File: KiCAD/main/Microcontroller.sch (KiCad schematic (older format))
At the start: 10 parts, among them J5 Conn_02x04_Odd_Even, SW2 BOOT, SW3 RESET, U3 ESP32-WROOM-32

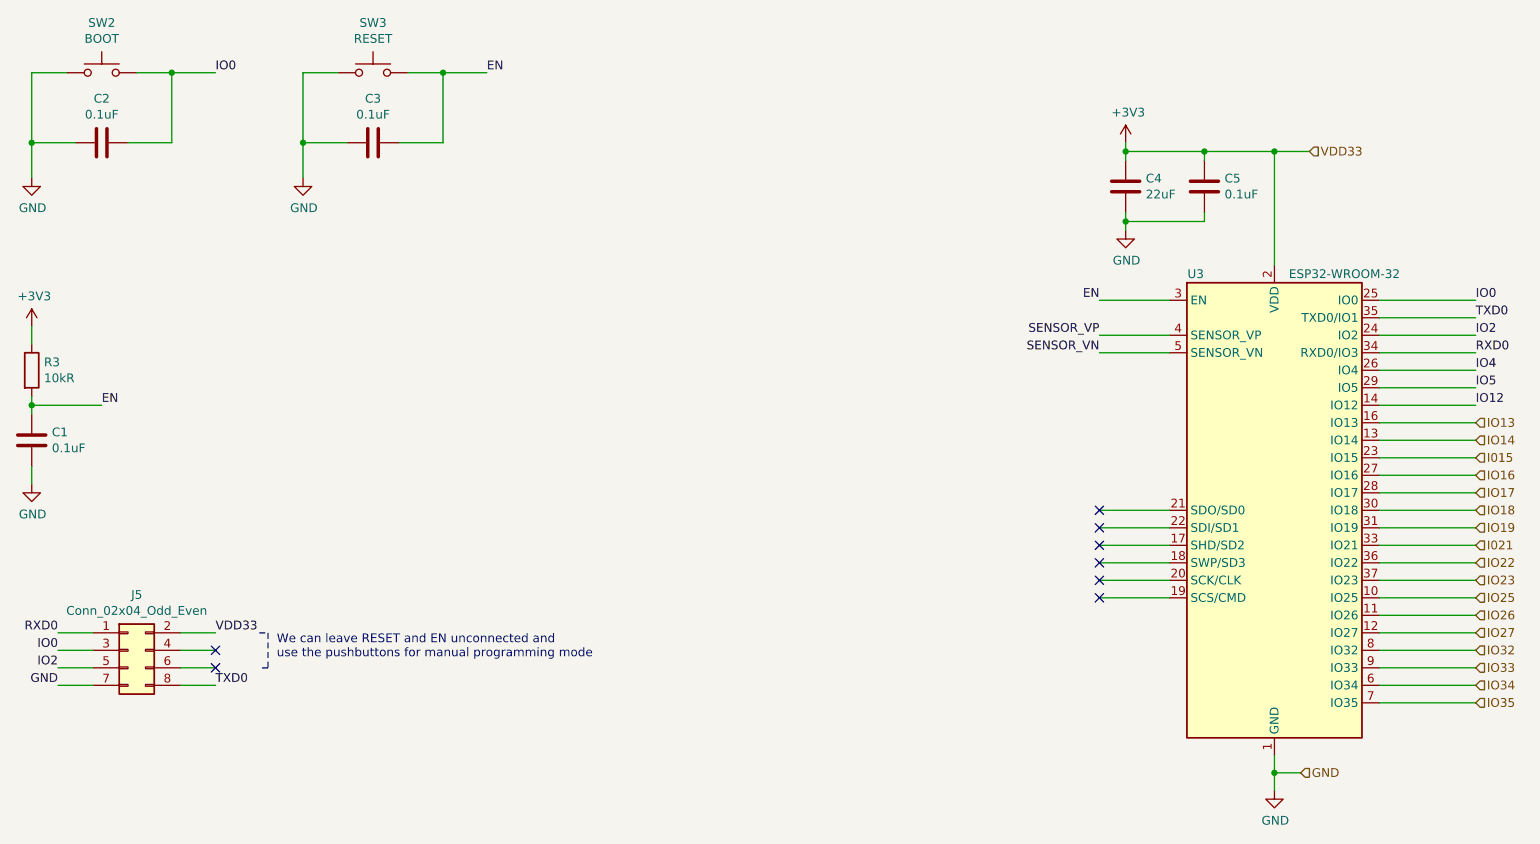
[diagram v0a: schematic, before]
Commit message: Improve EN circuit for microcontroller
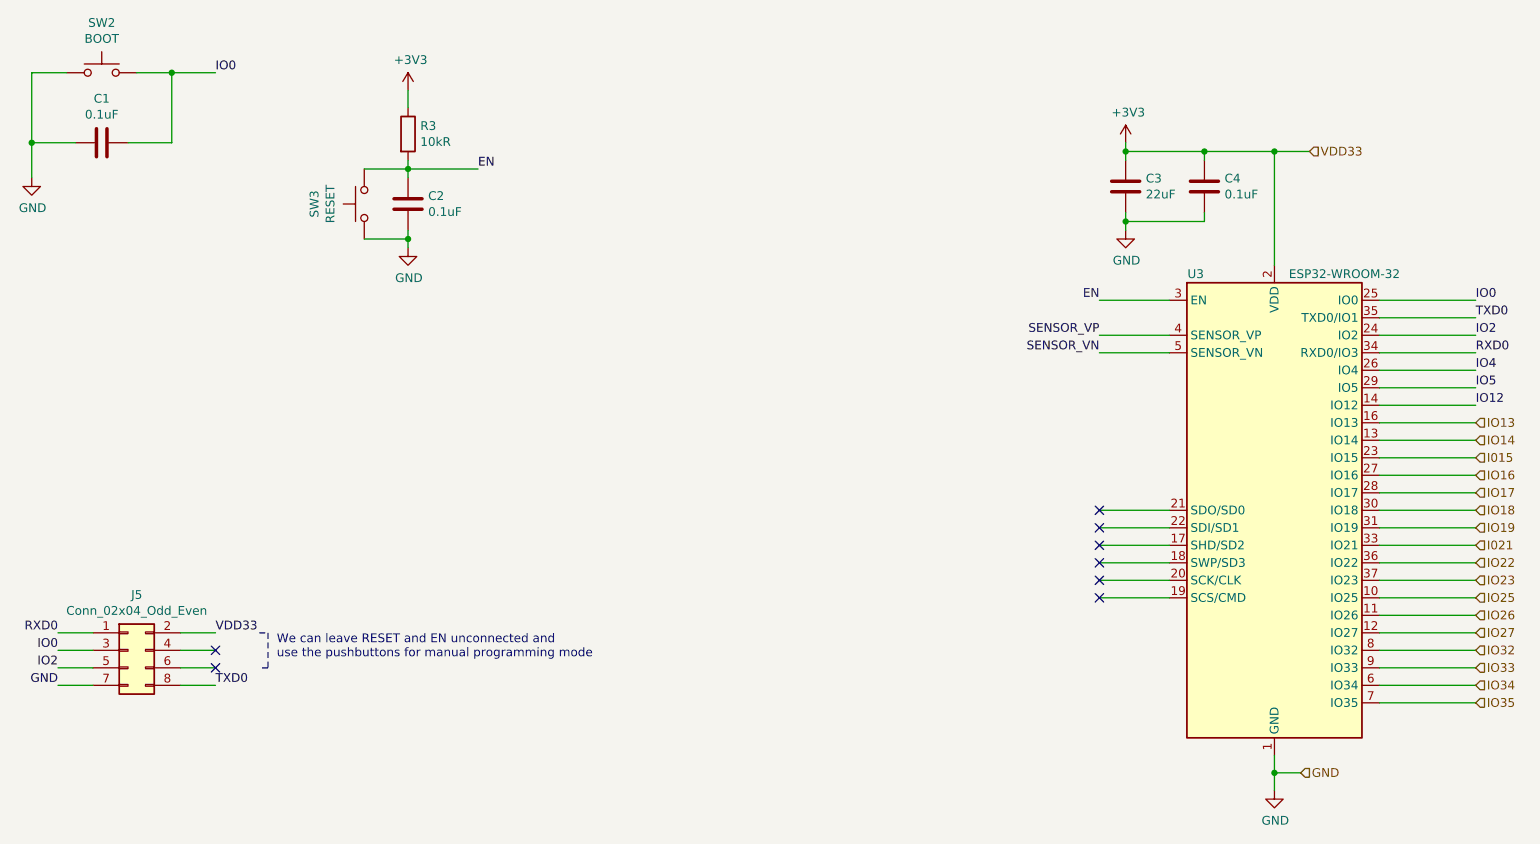
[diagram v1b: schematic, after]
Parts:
- removed C3: 0.1uF, Capacitor_SMD:C_1206_3216Metric, symbol Device:C
- renumbered C2 to C1, C1 to C2, C4 to C3, C5 to C4
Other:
- moved on the sheet: C2, R3, SW3
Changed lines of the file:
@@
 L power:+3V3 #PWR02
 U 1 1 5F9419AA
-P 1100 2650
-F 0 "#PWR02" H 1100 2500 50  0001 C CNN
-F 1 "+3V3" H 1115 2823 50  0000 C CNN
-F 2 "" H 1100 2650 50  0001 C CNN
-F 3 "" H 1100 2650 50  0001 C CNN
-	1    1100 2650
+P 3250 1300
+F 0 "#PWR02" H 3250 1150 50  0001 C CNN
+F 1 "+3V3" H 3265 1473 50  0000 C CNN
+F 2 "" H 3250 1300 50  0001 C CNN
+F 3 "" H 3250 1300 50  0001 C CNN
+	1    3250 1300
 	1    0    0    -1
 $EndComp
@@
 L Device:R R3
 U 1 1 5F94208F
-P 1100 2900
-F 0 "R3" H 1170 2946 50  0000 L CNN
-F 1 "10kR" H 1170 2855 50  0000 L CNN
-F 2 "Resistor_SMD:R_1206_3216Metric" V 1030 2900 50  0001 C CNN
-F 3 "~" H 1100 2900 50  0001 C CNN
-	1    1100 2900
-	1    0    0    -1
-$EndComp
-$Comp
-L Device:C C1
+P 3250 1550
+F 0 "R3" H 3320 1596 50  0000 L CNN
+F 1 "10kR" H 3320 1505 50  0000 L CNN
+F 2 "Resistor_SMD:R_1206_3216Metric" V 3180 1550 50  0001 C CNN
+F 3 "~" H 3250 1550 50  0001 C CNN
+	1    3250 1550
+	1    0    0    -1
+$EndComp
+$Comp
+L Device:C C2
 U 1 1 5F9429EB
-P 1100 3300
-F 0 "C1" H 1215 3346 50  0000 L CNN
-F 1 "0.1uF" H 1215 3255 50  0000 L CNN
-F 2 "Capacitor_SMD:C_1206_3216Metric" H 1138 3150 50  0001 C CNN
-F 3 "~" H 1100 3300 50  0001 C CNN
-F 4 "50V" H 1215 3255 50  0001 L CNN "Voltage"
-F 5 "10%" H 1215 3164 50  0001 L CNN "Tolerance"
-	1    1100 3300
+P 3250 1950
+F 0 "C2" H 3365 1996 50  0000 L CNN
+F 1 "0.1uF" H 3365 1905 50  0000 L CNN
+F 2 "Capacitor_SMD:C_1206_3216Metric" H 3288 1800 50  0001 C CNN
+F 3 "~" H 3250 1950 50  0001 C CNN
+F 4 "50V" H 3365 1905 50  0001 L CNN "Voltage"
+F 5 "10%" H 3365 1814 50  0001 L CNN "Tolerance"
+	1    3250 1950
 	1    0    0    -1
 $EndComp
@@
 L power:GND #PWR03
 U 1 1 5F942C61
-P 1100 3550
-F 0 "#PWR03" H 1100 3300 50  0001 C CNN
-F 1 "GND" H 1105 3377 50  0000 C CNN
-F 2 "" H 1100 3550 50  0001 C CNN
-F 3 "" H 1100 3550 50  0001 C CNN
-	1    1100 3550
-	1    0    0    -1
-$EndComp
-Wire Wire Line
-	1100 3550 1100 3450
-Wire Wire Line
-	1100 2750 1100 2650
-$Comp
-L power:+3V3 #PWR05
+P 3250 2200
+F 0 "#PWR03" H 3250 1950 50  0001 C CNN
+F 1 "GND" H 3255 2027 50  0000 C CNN
+F 2 "" H 3250 2200 50  0001 C CNN
+F 3 "" H 3250 2200 50  0001 C CNN
+	1    3250 2200
+	1    0    0    -1
+$EndComp
+Wire Wire Line
+	3250 2200 3250 2150
+Wire Wire Line
+	3250 1400 3250 1300
+$Comp
+L power:+3V3 #PWR04
 U 1 1 5F943FB0
 P 7350 1600
-F 0 "#PWR05" H 7350 1450 50  0001 C CNN
+F 0 "#PWR04" H 7350 1450 50  0001 C CNN
 F 1 "+3V3" H 7365 1773 50  0000 C CNN
 F 2 "" H 7350 1600 50  0001 C CNN
@@
 $EndComp
 $Comp
-L Device:C C5
+L Device:C C4
 U 1 1 5F9451F0
 P 7800 1850
-F 0 "C5" H 7915 1896 50  0000 L CNN
+F 0 "C4" H 7915 1896 50  0000 L CNN
 F 1 "0.1uF" H 7915 1805 50  0000 L CNN
 F 2 "Capacitor_SMD:C_1206_3216Metric" H 7838 1700 50  0001 C CNN
@@
 $EndComp
 $Comp
-L Device:C C4
+L Device:C C3
 U 1 1 5F946123
 P 7350 1850
-F 0 "C4" H 7465 1896 50  0000 L CNN
+F 0 "C3" H 7465 1896 50  0000 L CNN
 F 1 "22uF" H 7465 1805 50  0000 L CNN
 F 2 "Capacitor_SMD:C_1206_3216Metric" H 7388 1700 50  0001 C CNN
@@
 	7350 2050 7350 2000
 $Comp
-L power:GND #PWR06
+L power:GND #PWR05
 U 1 1 5F947B11
 P 7350 2100
-F 0 "#PWR06" H 7350 1850 50  0001 C CNN
+F 0 "#PWR05" H 7350 1850 50  0001 C CNN
 F 1 "GND" H 7355 1927 50  0000 C CNN
 F 2 "" H 7350 2100 50  0001 C CNN
@@
 	8200 2300 8200 1650
 $Comp
-L power:GND #PWR07
+L power:GND #PWR06
 U 1 1 5F95286C
 P 8200 5300
-F 0 "#PWR07" H 8200 5050 50  0001 C CNN
+F 0 "#PWR06" H 8200 5050 50  0001 C CNN
 F 1 "GND" H 8205 5127 50  0000 C CNN
 F 2 "" H 8200 5300 50  0001 C CNN
@@
 $EndComp
 $Comp
-L Device:C C2
+L Device:C C1
 U 1 1 5F9586F2
 P 1500 1600
-F 0 "C2" V 1752 1600 50  0000 C CNN
+F 0 "C1" V 1752 1600 50  0000 C CNN
 F 1 "0.1uF" V 1661 1600 50  0000 C CNN
 F 2 "Capacitor_SMD:C_1206_3216Metric" H 1538 1450 50  0001 C CNN
@@
 Connection ~ 1900 1200
 $Comp
-L power:GND #PWR04
-U 1 1 5F960D2F
-P 2650 1800
-F 0 "#PWR04" H 2650 1550 50  0001 C CNN
-F 1 "GND" H 2655 1627 50  0000 C CNN
-F 2 "" H 2650 1800 50  0001 C CNN
-F 3 "" H 2650 1800 50  0001 C CNN
-	1    2650 1800
-	1    0    0    -1
-$EndComp
-$Comp
-L Device:C C3
-U 1 1 5F960D36
-P 3050 1600
-F 0 "C3" V 3302 1600 50  0000 C CNN
-F 1 "0.1uF" V 3211 1600 50  0000 C CNN
-F 2 "Capacitor_SMD:C_1206_3216Metric" H 3088 1450 50  0001 C CNN
-F 3 "~" H 3050 1600 50  0001 C CNN
-F 4 "50V" V 3050 1600 50  0001 C CNN "Voltage"
-	1    3050 1600
-	0    -1   -1   0
-$EndComp
-Wire Wire Line
-	2900 1600 2650 1600
-Wire Wire Line
-	2650 1600 2650 1800
-$Comp
 L Switch:SW_Push SW3
 U 1 1 5F960D3E
-P 3050 1200
-F 0 "SW3" H 3050 1485 50  0000 C CNN
-F 1 "RESET" H 3050 1394 50  0000 C CNN
-F 2 "Button_Switch_SMD:SW_SPST_PTS645" H 3050 1400 50  0001 C CNN
-F 3 "~" H 3050 1400 50  0001 C CNN
-	1    3050 1200
-	1    0    0    -1
-$EndComp
-Wire Wire Line
-	2850 1200 2650 1200
-Wire Wire Line
-	2650 1200 2650 1600
-Connection ~ 2650 1600
-Wire Wire Line
-	3200 1600 3450 1600
-Wire Wire Line
-	3450 1600 3450 1200
-Wire Wire Line
-	3450 1200 3250 1200
-Text Label 3700 1200 0    50   ~ 0
-EN
-Wire Wire Line
-	3450 1200 3700 1200
-Connection ~ 3450 1200
-Wire Wire Line
-	1100 3050 1100 3100
-Connection ~ 1100 3100
-Wire Wire Line
-	1100 3100 1100 3150
-Wire Wire Line
-	1100 3100 1500 3100
+P 3000 1950
+F 0 "SW3" H 3000 2235 50  0000 C CNN
+F 1 "RESET" H 3000 2144 50  0000 C CNN
+F 2 "Button_Switch_SMD:SW_SPST_PTS645" H 3000 2150 50  0001 C CNN
+F 3 "~" H 3000 2150 50  0001 C CNN
+	1    3000 1950
+	0    -1   -1   0
+$EndComp
+Wire Wire Line
+	3250 1700 3250 1750
+Connection ~ 3250 1750
+Wire Wire Line
+	3250 1750 3250 1800
+Wire Wire Line
+	3250 1750 3650 1750
 Wire Wire Line
 	8800 2900 9350 2900
@@
 Wire Wire Line
 	7200 2500 7600 2500
-Text Label 1500 3100 0    50   ~ 0
+Text Label 3650 1750 0    50   ~ 0
 EN
 Text HLabel 8400 1650 2    50   Input ~ 0
@@
 Text HLabel 9350 3200 2    50   Input ~ 0
 IO13
+Wire Wire Line
+	3000 1750 3250 1750
+Wire Wire Line
+	3250 2150 3000 2150
+Connection ~ 3250 2150
+Wire Wire Line
+	3250 2150 3250 2100
 $EndSCHEMATC

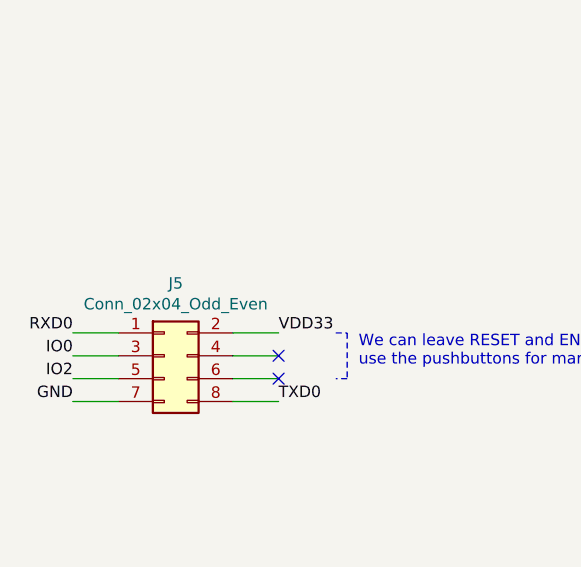
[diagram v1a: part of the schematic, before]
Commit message: Fix battery charger connectors
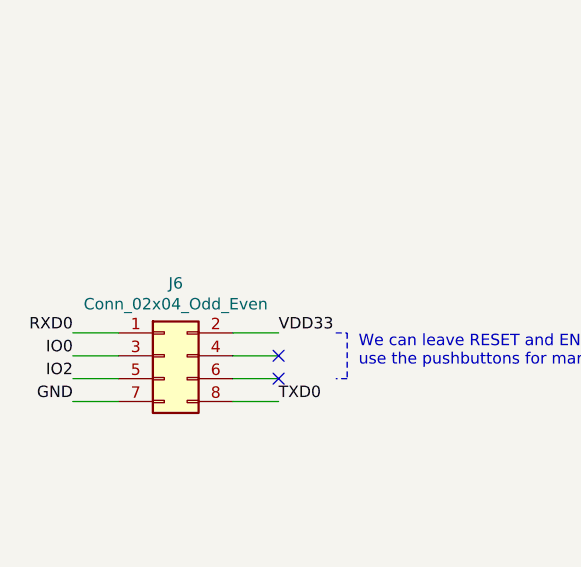
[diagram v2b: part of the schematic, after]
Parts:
- renumbered J5 to J6
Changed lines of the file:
@@
 TXD0
 $Comp
-L Connector_Generic:Conn_02x04_Odd_Even J5
+L Connector_Generic:Conn_02x04_Odd_Even J6
 U 1 1 5FC4BA04
 P 1650 4500
-F 0 "J5" H 1700 4817 50  0000 C CNN
+F 0 "J6" H 1700 4817 50  0000 C CNN
 F 1 "Conn_02x04_Odd_Even" H 1700 4726 50  0000 C CNN
 F 2 "Connector_PinHeader_2.54mm:PinHeader_2x04_P2.54mm_Vertical" H 1650 4500 50  0001 C CNN

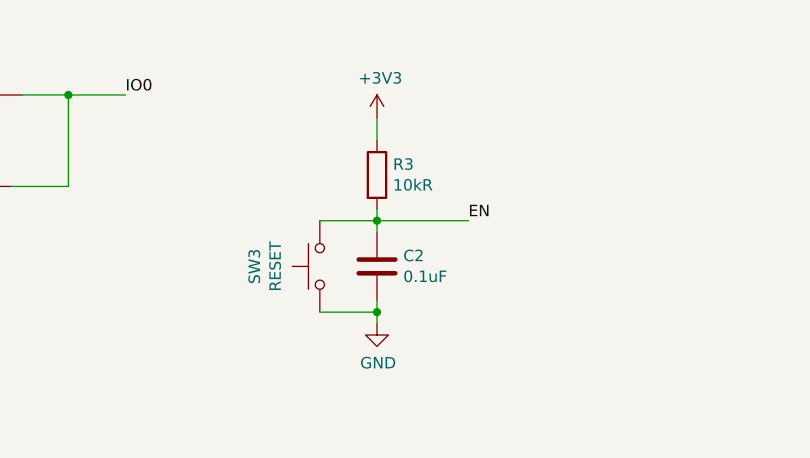
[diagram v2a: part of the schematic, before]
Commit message: Preliminary layout with fixed component pins
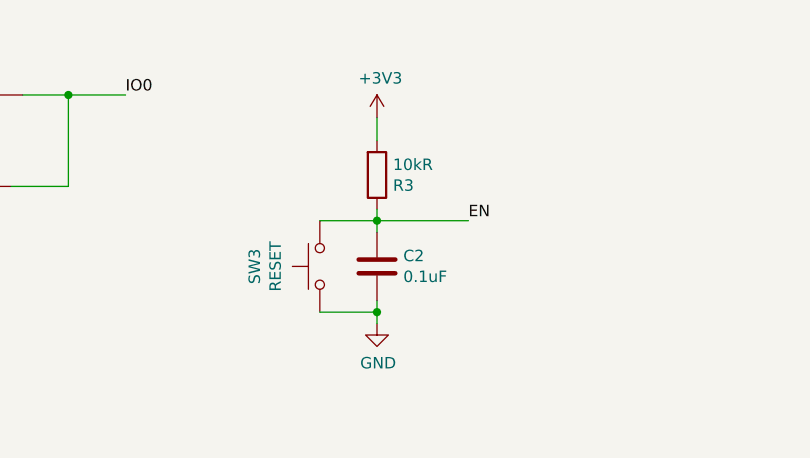
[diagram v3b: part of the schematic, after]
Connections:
- net +3V3: now also R3.2; no longer R3.1
- net EN: now also R3.1; no longer R3.2
- net GND: now also C1.2; no longer C1.1
- net IO0: now also C1.1; no longer C1.2
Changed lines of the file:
@@
 F 3 "~" H 3250 1550 50  0001 C CNN
 	1    3250 1550
-	1    0    0    -1
+	1    0    0    1
 $EndComp
 $Comp
@@
 F 4 "50V" V 1500 1600 50  0001 C CNN "Voltage"
 	1    1500 1600
-	0    -1   -1   0
+	0    1    -1   0
 $EndComp
 Wire Wire Line

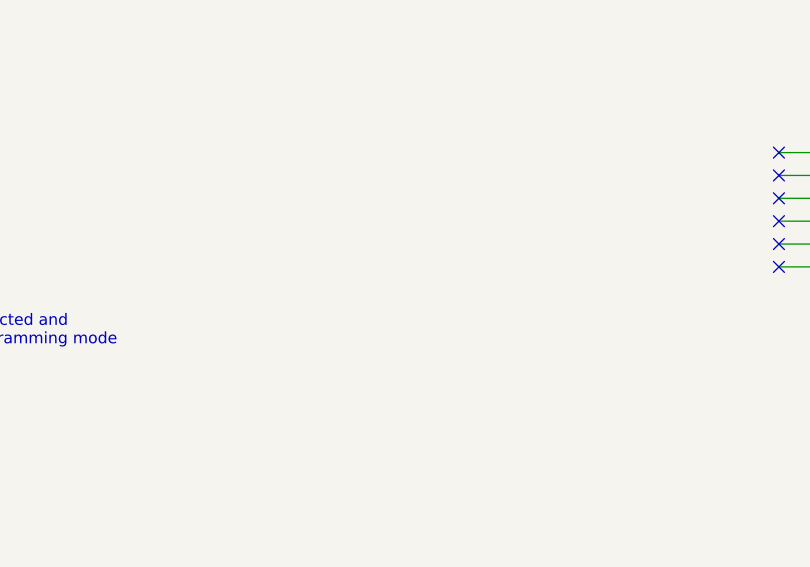
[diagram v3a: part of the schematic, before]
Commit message: Add some pcb test points
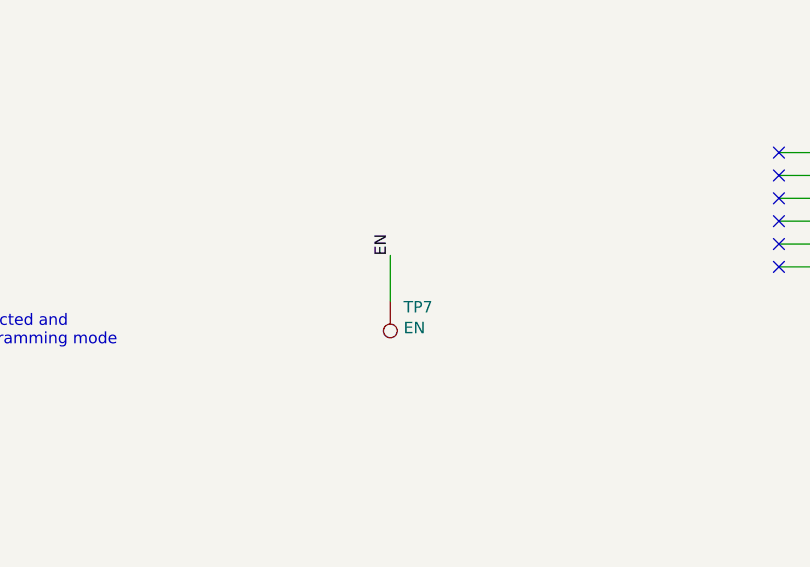
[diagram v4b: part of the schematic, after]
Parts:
- added TP7: EN, TestPoint:TestPoint_Pad_1.0x1.0mm, symbol Connector:TestPoint
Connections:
- net EN: now also TP7.1
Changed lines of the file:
@@
 Wire Wire Line
 	3250 2150 3250 2100
+$Comp
+L Connector:TestPoint TP?
+U 1 1 5FDE9445
+P 5500 4350
+AR Path="/5FDE9445" Ref="TP?"  Part="1"
+AR Path="/5F928E95/5FDE9445" Ref="TP7"  Part="1"
+F 0 "TP7" H 5442 4376 50  0000 R CNN
+F 1 "EN" H 5442 4467 50  0000 R CNN
+F 2 "TestPoint:TestPoint_Pad_1.0x1.0mm" H 5700 4350 50  0001 C CNN
+F 3 "~" H 5700 4350 50  0001 C CNN
+	1    5500 4350
+	-1   0    0    1
+$EndComp
+Wire Wire Line
+	5500 4350 5500 4150
+Text Label 5500 4150 1    50   ~ 0
+EN
 $EndSCHEMATC

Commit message: Replace all possible footprints to THT variants
Also clear current PCB design and update component footprints
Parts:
- C1, C2, C4: footprint Capacitor_SMD:C_1206_3216Metric -> Capacitor_THT:C_Disc_D4.3mm_W1.9mm_P5.00mm
- C3: footprint Capacitor_SMD:C_1206_3216Metric -> Capacitor_THT:CP_Radial_D6.3mm_P2.50mm; symbol Device:C -> Device:CP
- R3: footprint Resistor_SMD:R_1206_3216Metric -> Resistor_THT:R_Axial_DIN0207_L6.3mm_D2.5mm_P10.16mm_Horizontal
- SW2, SW3: footprint Button_Switch_SMD:SW_SPST_PTS645 -> Button_Switch_THT:SW_PUSH_6mm
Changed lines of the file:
@@
 F 0 "R3" H 3320 1596 50  0000 L CNN
 F 1 "10kR" H 3320 1505 50  0000 L CNN
-F 2 "Resistor_SMD:R_1206_3216Metric" V 3180 1550 50  0001 C CNN
+F 2 "Resistor_THT:R_Axial_DIN0207_L6.3mm_D2.5mm_P10.16mm_Horizontal" V 3180 1550 50  0001 C CNN
 F 3 "~" H 3250 1550 50  0001 C CNN
 	1    3250 1550
@@
 F 0 "C2" H 3365 1996 50  0000 L CNN
 F 1 "0.1uF" H 3365 1905 50  0000 L CNN
-F 2 "Capacitor_SMD:C_1206_3216Metric" H 3288 1800 50  0001 C CNN
+F 2 "Capacitor_THT:C_Disc_D4.3mm_W1.9mm_P5.00mm" H 3288 1800 50  0001 C CNN
 F 3 "~" H 3250 1950 50  0001 C CNN
 F 4 "50V" H 3365 1905 50  0001 L CNN "Voltage"
@@
 F 0 "C4" H 7915 1896 50  0000 L CNN
 F 1 "0.1uF" H 7915 1805 50  0000 L CNN
-F 2 "Capacitor_SMD:C_1206_3216Metric" H 7838 1700 50  0001 C CNN
+F 2 "Capacitor_THT:C_Disc_D4.3mm_W1.9mm_P5.00mm" H 7838 1700 50  0001 C CNN
 F 3 "~" H 7800 1850 50  0001 C CNN
 F 4 "50V" H 7915 1759 50  0001 L CNN "Voltage"
@@
 $EndComp
 $Comp
-L Device:C C3
+L Device:CP C3
 U 1 1 5F946123
 P 7350 1850
 F 0 "C3" H 7465 1896 50  0000 L CNN
 F 1 "22uF" H 7465 1805 50  0000 L CNN
-F 2 "Capacitor_SMD:C_1206_3216Metric" H 7388 1700 50  0001 C CNN
+F 2 "Capacitor_THT:CP_Radial_D6.3mm_P2.50mm" H 7388 1700 50  0001 C CNN
 F 3 "~" H 7350 1850 50  0001 C CNN
 F 4 "10V" H 7465 1759 50  0001 L CNN "Voltage"
@@
 F 0 "C1" V 1752 1600 50  0000 C CNN
 F 1 "0.1uF" V 1661 1600 50  0000 C CNN
-F 2 "Capacitor_SMD:C_1206_3216Metric" H 1538 1450 50  0001 C CNN
+F 2 "Capacitor_THT:C_Disc_D4.3mm_W1.9mm_P5.00mm" H 1538 1450 50  0001 C CNN
 F 3 "~" H 1500 1600 50  0001 C CNN
 F 4 "50V" V 1500 1600 50  0001 C CNN "Voltage"
@@
 F 0 "SW2" H 1500 1485 50  0000 C CNN
 F 1 "BOOT" H 1500 1394 50  0000 C CNN
-F 2 "Button_Switch_SMD:SW_SPST_PTS645" H 1500 1400 50  0001 C CNN
+F 2 "Button_Switch_THT:SW_PUSH_6mm" H 1500 1400 50  0001 C CNN
 F 3 "~" H 1500 1400 50  0001 C CNN
 	1    1500 1200
@@
 F 0 "SW3" H 3000 2235 50  0000 C CNN
 F 1 "RESET" H 3000 2144 50  0000 C CNN
-F 2 "Button_Switch_SMD:SW_SPST_PTS645" H 3000 2150 50  0001 C CNN
+F 2 "Button_Switch_THT:SW_PUSH_6mm" H 3000 2150 50  0001 C CNN
 F 3 "~" H 3000 2150 50  0001 C CNN
 	1    3000 1950

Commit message: Expand design vertically, reposition components and re-track
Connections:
- net GND: now also C1.1, SW2.2; no longer C1.2, SW2.1
- net IO0: now also C1.2, SW2.1; no longer C1.1, SW2.2
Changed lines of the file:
@@
 F 4 "50V" V 1500 1600 50  0001 C CNN "Voltage"
 	1    1500 1600
-	0    1    -1   0
+	0    -1   -1   0
 $EndComp
 Wire Wire Line
@@
 F 3 "~" H 1500 1400 50  0001 C CNN
 	1    1500 1200
-	1    0    0    -1
+	-1   0    0    -1
 $EndComp
 Wire Wire Line

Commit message: increase via pad to 1.1mm and allow space for fixtures
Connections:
- net GND: now also SW2.1; no longer SW2.2
- net IO0: now also SW2.2; no longer SW2.1
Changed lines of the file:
@@
-	1    0    0    -1
-$EndComp
-$Comp
-L Device:CP C3
-U 1 1 5F946123
-P 7350 1850
-F 0 "C3" H 7465 1896 50  0000 L CNN
-F 1 "22uF" H 7465 1805 50  0000 L CNN
-F 2 "Capacitor_THT:CP_Radial_D6.3mm_P2.50mm" H 7388 1700 50  0001 C CNN
-F 3 "~" H 7350 1850 50  0001 C CNN
-F 4 "10V" H 7465 1759 50  0001 L CNN "Voltage"
-	1    7350 1850
 	1    0    0    -1
 $EndComp
@@
 F 3 "~" H 1500 1400 50  0001 C CNN
 	1    1500 1200
-	-1   0    0    -1
+	1    0    0    -1
 $EndComp
 Wire Wire Line
@@
 Text Label 5500 4150 1    50   ~ 0
 EN
+$Comp
+L Device:CP C3
+U 1 1 5F946123
+P 7350 1850
+F 0 "C3" H 7465 1896 50  0000 L CNN
+F 1 "22uF" H 7465 1805 50  0000 L CNN
+F 2 "Capacitor_THT:CP_Radial_D6.3mm_P2.50mm" H 7388 1700 50  0001 C CNN
+F 3 "~" H 7350 1850 50  0001 C CNN
+F 4 "10V" H 7465 1759 50  0001 L CNN "Voltage"
+	1    7350 1850
+	1    0    0    -1
+$EndComp
 $EndSCHEMATC
